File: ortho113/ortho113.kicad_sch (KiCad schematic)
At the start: 1 part, among them U1 RP2350_Stamp_XL

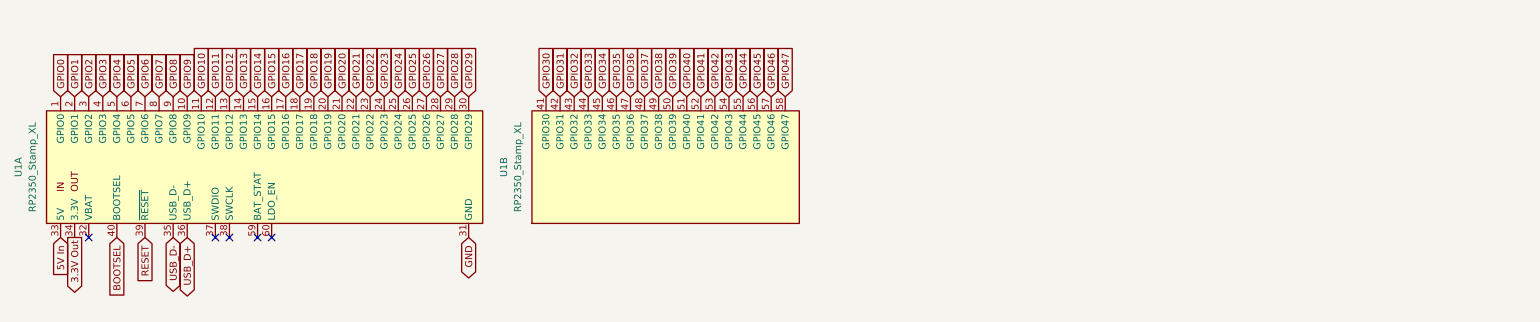
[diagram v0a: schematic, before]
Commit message: fixed unlinked schematic and pcb files
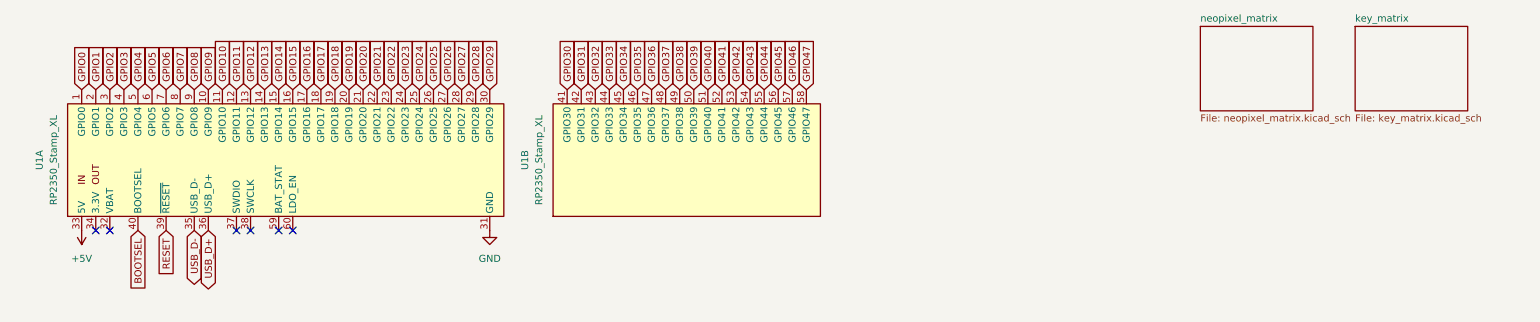
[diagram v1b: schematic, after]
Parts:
- U1: footprint (none) -> RP2xxx_Stamp:RP2xxx_Stamp_XL_THT
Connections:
- net 3.3V Out: no longer names the net of U1.34 (3.3V)
- net 5V In renamed +5V
- no-connect marks 5 -> 6
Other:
- added sheet key_matrix (key_matrix.kicad_sch)
- added sheet neopixel_matrix (neopixel_matrix.kicad_sch)

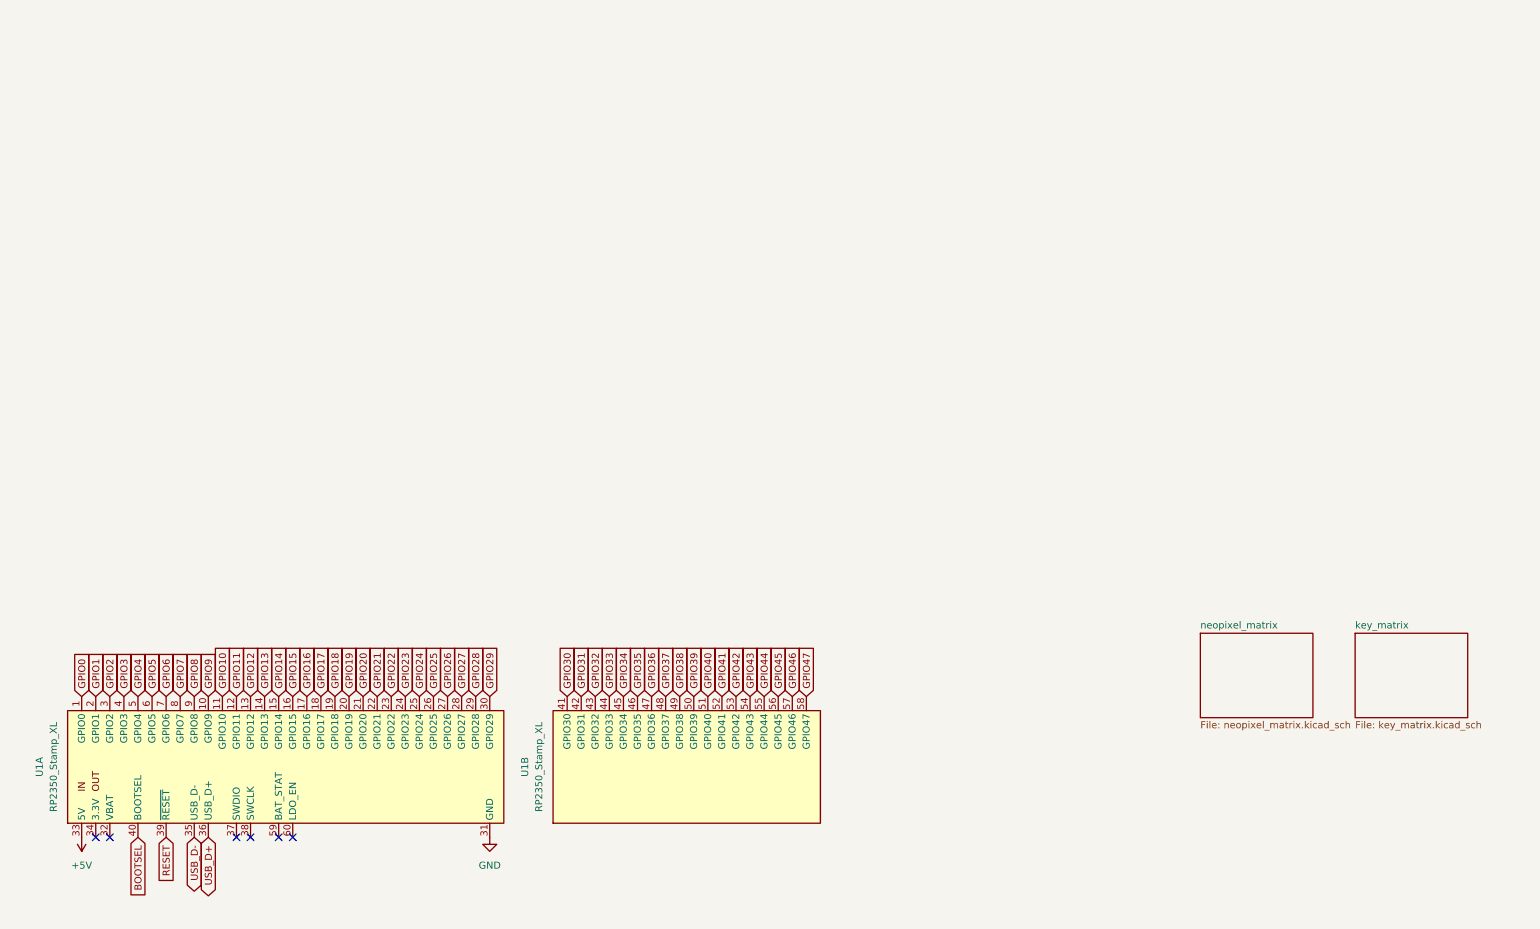
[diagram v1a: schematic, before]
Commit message: fixed submodule conflict & remove gitignore
added pinout for oled display
finished rev1 of pcb design
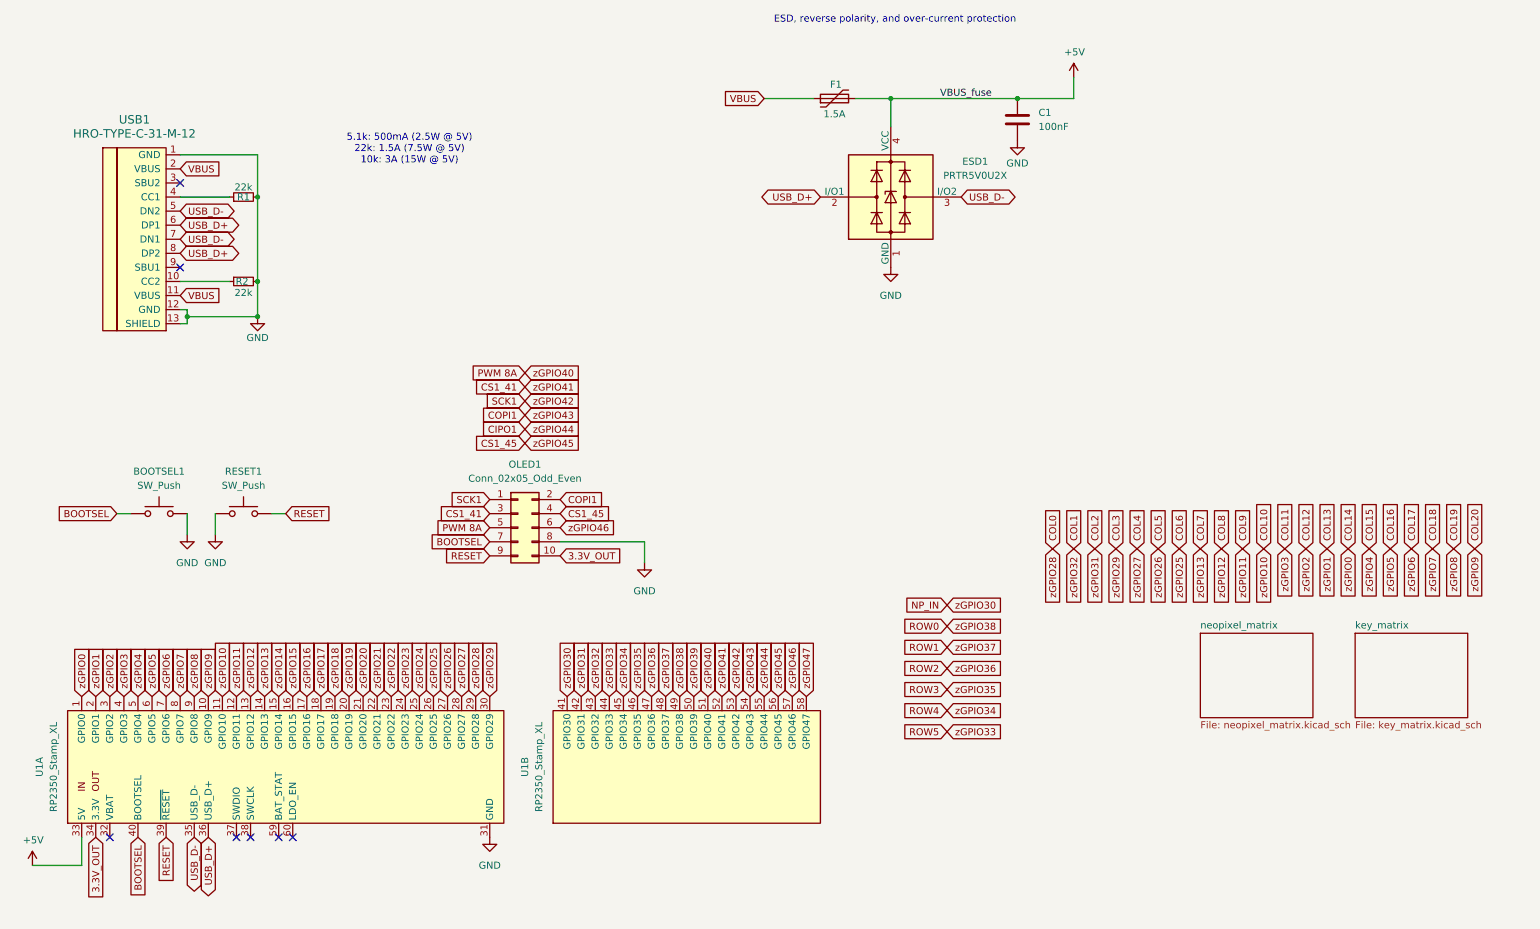
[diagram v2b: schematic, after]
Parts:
- added BOOTSEL1, RESET1: SW_Push, Button_Switch_SMD:SW_SPST_TL3342, symbol Switch:SW_Push
- added C1: 100nF, Capacitor_SMD:C_0402_1005Metric_Pad0.74x0.62mm_HandSolder, symbol Device:C
- added ESD1: PRTR5V0U2X, Package_TO_SOT_SMD:SOT-143, symbol Power_Protection:PRTR5V0U2X
- added F1: 1.5A, Fuse:Fuse_1206_3216Metric, symbol Device:Polyfuse
- added OLED1: Conn_02x05_Odd_Even, Connector_PinHeader_2.54mm:PinHeader_2x05_P2.54mm_Vertical_SMD, symbol Connector_Generic:Conn_02x05_Odd_Even
- added R1, R2: 22k, Resistor_SMD:R_1812_4532Metric_Pad1.30x3.40mm_HandSolder, symbol Device:R_Small
- added USB1: HRO-TYPE-C-31-M-12, my-footprints:HRO-TYPE-C-31-M-12-HandSoldering, symbol Type-C:HRO-TYPE-C-31-M-12
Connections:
- net +5V: now also C1.1, ESD1.4 (VCC), F1.2
- net BOOTSEL: now also BOOTSEL1.1, OLED1.7 (Pin_7)
- net GND: now also BOOTSEL1.2, C1.2, ESD1.1 (GND), OLED1.8 (Pin_8), R1.2, R2.2, RESET1.1, USB1.1 (GND), USB1.12 (GND), USB1.13 (SHIELD)
- net RESET: now also OLED1.9 (Pin_9), RESET1.2
- net USB_D+: now also ESD1.2 (I/O1), USB1.6 (DP1), USB1.8 (DP2)
- net USB_D-: now also ESD1.3 (I/O2), USB1.5 (DN2), USB1.7 (DN1)
- net 3.3V_OUT: now reaches U1.34 (3.3V)
- net 3.3V_OUT: now also OLED1.10 (Pin_10)
- net GPIO0 renamed COL14
- net GPIO1 renamed COL13
- net GPIO10 renamed COL10
- net GPIO11 renamed COL9
- net GPIO12 renamed COL8
- net GPIO13 renamed COL7
- net GPIO14 renamed zGPIO14
- net GPIO15 renamed zGPIO15
- net GPIO16 renamed zGPIO16
- net GPIO17 renamed zGPIO17
- net GPIO18 renamed zGPIO18
- net GPIO19 renamed zGPIO19
- net GPIO2 renamed COL12
- net GPIO20 renamed zGPIO20
- net GPIO21 renamed zGPIO21
- net GPIO22 renamed zGPIO22
- net GPIO23 renamed zGPIO23
- net GPIO24 renamed zGPIO24
- net GPIO25 renamed COL6
- net GPIO26 renamed COL5
- net GPIO27 renamed COL4
- net GPIO28 renamed COL0
- net GPIO29 renamed COL3
- net GPIO3 renamed COL11
- net GPIO30 renamed NP_IN
- net GPIO31 renamed COL2
- net GPIO32 renamed COL1
- net GPIO33 renamed ROW5
- net GPIO34 renamed ROW4
- net GPIO35 renamed ROW3
- net GPIO36 renamed ROW2
- net GPIO37 renamed ROW1
- net GPIO38 renamed ROW0
- net GPIO39 renamed zGPIO39
- net GPIO4 renamed COL15
- net GPIO40 renamed PWM 8A
- net PWM 8A: now also OLED1.5 (Pin_5)
- net GPIO41 renamed CS1_41
- net CS1_41: now also OLED1.3 (Pin_3)
- net GPIO42 renamed SCK1
- net SCK1: now also OLED1.1 (Pin_1)
- net GPIO43 renamed COPI1
- net COPI1: now also OLED1.2 (Pin_2)
- net GPIO44 renamed CIPO1
- net GPIO45 renamed CS1_45
- net CS1_45: now also OLED1.4 (Pin_4)
- net GPIO46 renamed zGPIO46
- net zGPIO46: now also OLED1.6 (Pin_6)
- net GPIO47 renamed zGPIO47
- net GPIO5 renamed COL16
- net GPIO6 renamed COL17
- net GPIO7 renamed COL18
- net GPIO8 renamed COL19
- net GPIO9 renamed COL20
- new net: R2.1, USB1.10 (CC2)
- new net: R1.1, USB1.4 (CC1)
- new net VBUS: F1.1, USB1.11 (VBUS), USB1.2 (VBUS)
- no-connect marks 6 -> 7
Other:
- note added: "5.1k: 500mA (2.5W @ 5V) 22k: 1.5A (7.5W @ 5V) 10k: 3A (15W @ 5V)"
- note added: "ESD, reverse polarity, and over-current protection"
